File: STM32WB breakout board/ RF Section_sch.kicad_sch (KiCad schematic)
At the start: 12 parts, among them J3 RSP-122811-02

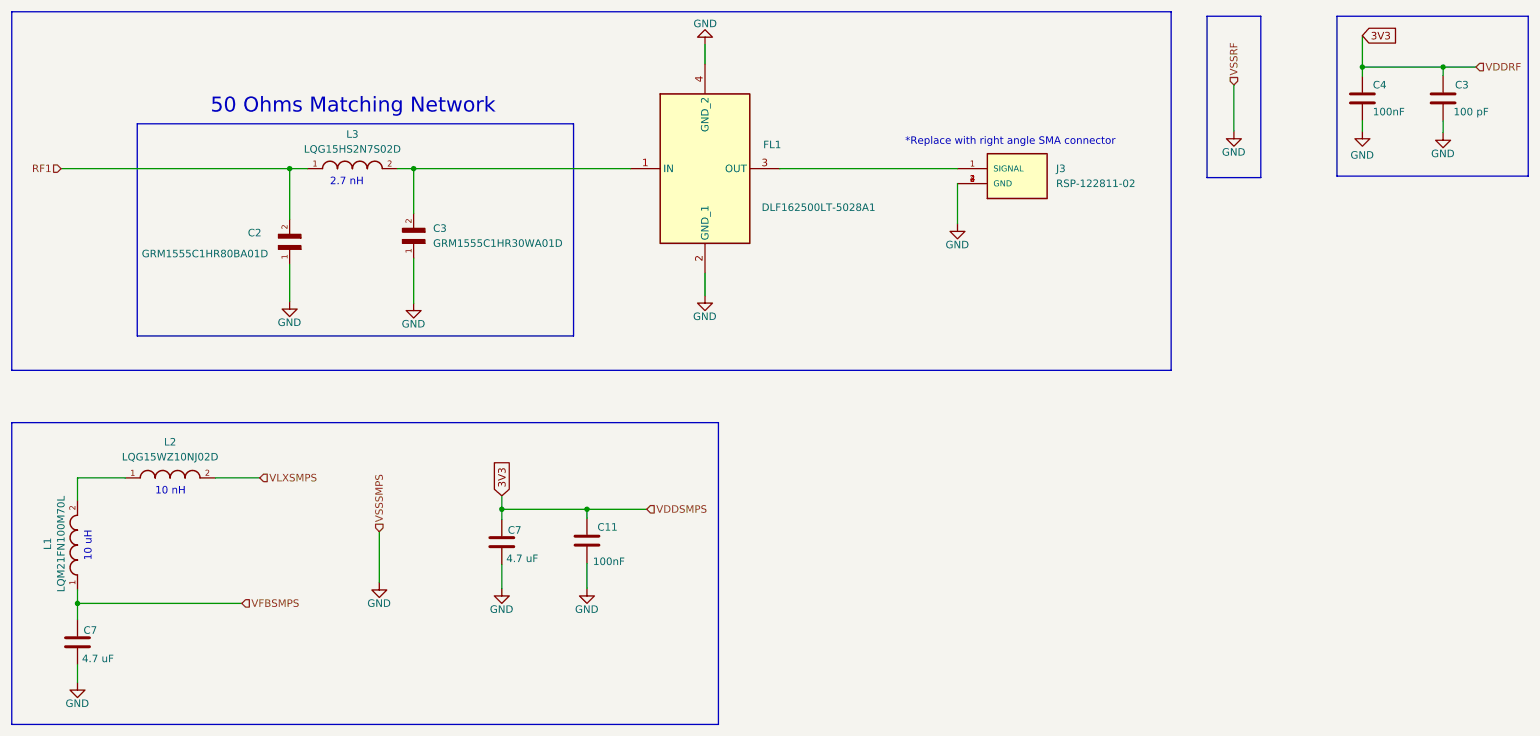
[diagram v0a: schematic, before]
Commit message: Regulator section updating
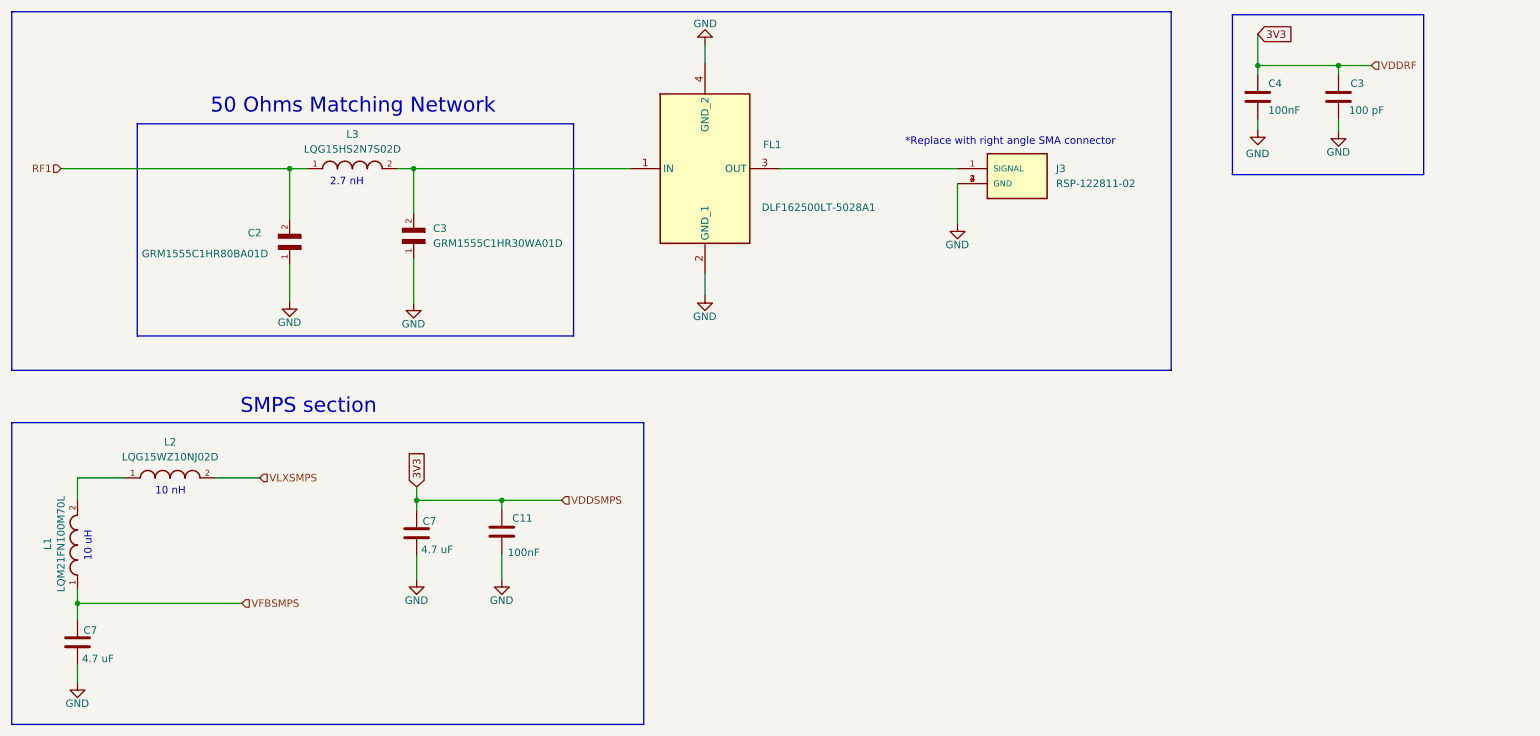
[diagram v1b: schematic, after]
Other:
- note added: "SMPS section"
- moved on the sheet: C11, C3, C4, C7

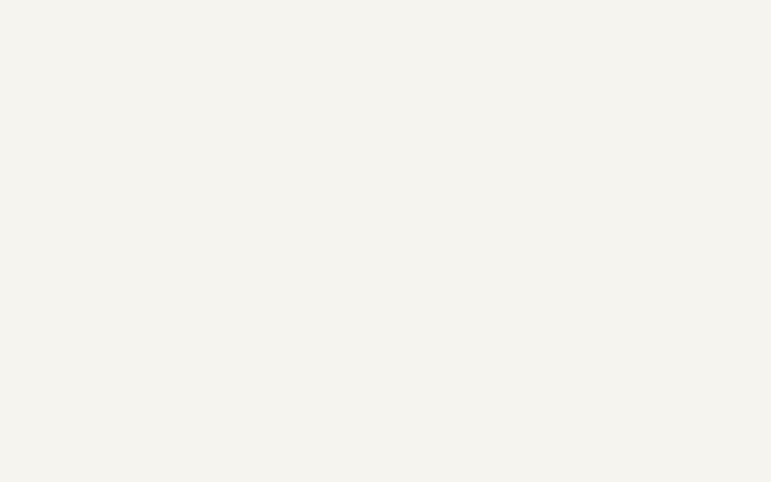
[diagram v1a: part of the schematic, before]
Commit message: Regulator section updating
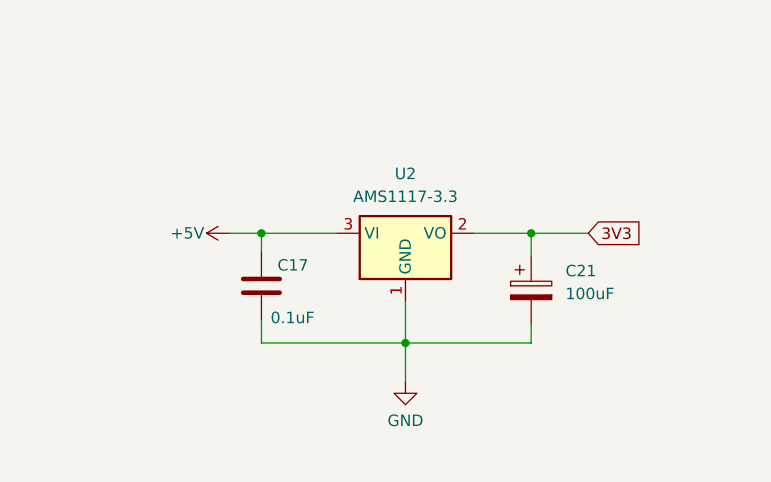
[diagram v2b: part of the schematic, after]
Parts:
- added C17: 0.1uF, Capacitor_SMD:C_0402_1005Metric, symbol Device:C
- added C21: 100uF, symbol Device:C_Polarized
- added U2: AMS1117-3.3, Package_TO_SOT_SMD:SOT-223-3_TabPin2, symbol Regulator_Linear:AMS1117-3.3
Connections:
- net 3V3: now also C21.1, U2.2 (VO)
- net GND: now also C17.2, C21.2, U2.1 (GND)
- new net +5V: C17.1, U2.3 (VI)
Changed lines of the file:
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@@
   (junction (at 68.072 46.99) (diameter 0) (color 0 0 0 0)
   )
+  (junction (at 236.22 115.824) (diameter 0) (color 0 0 0 0)
+  )
   (junction (at 89.154 46.99) (diameter 0) (color 0 0 0 0)
   )
   (junction (at 232.664 29.464) (diameter 0) (color 0 0 0 0)
   )
+  (junction (at 222.25 128.016) (diameter 0) (color 0 0 0 0)
+  )
+  (junction (at 206.248 115.824) (diameter 0) (color 0 0 0 0)
+  )
   (junction (at 89.662 103.378) (diameter 0) (color 0 0 0 0)
   )
@@
     (stroke (width 0) (type default))
   )
+  (wire (pts (xy 214.63 115.824) (xy 206.248 115.824))
+    (stroke (width 0) (type default))
+  )
   (wire (pts (xy 89.154 46.99) (xy 125.984 46.99))
     (stroke (width 0) (type default))
@@
     (stroke (width 0) (type default))
   )
+  (wire (pts (xy 202.692 115.824) (xy 206.248 115.824))
+    (stroke (width 0) (type default))
+  )
   (wire (pts (xy 232.664 38.608) (xy 232.664 40.386))
     (stroke (width 0) (type default))
@@
     (stroke (width 0) (type default))
   )
+  (wire (pts (xy 236.22 115.824) (xy 229.87 115.824))
+    (stroke (width 0) (type default))
+  )
   (wire (pts (xy 138.684 25.908) (xy 138.684 29.21))
     (stroke (width 0) (type default))
@@
     (stroke (width 0) (type default))
   )
+  (wire (pts (xy 206.248 128.016) (xy 222.25 128.016))
+    (stroke (width 0) (type default))
+  )
   (wire (pts (xy 89.154 62.23) (xy 89.154 69.85))
     (stroke (width 0) (type default))
@@
     (stroke (width 0) (type default))
   )
+  (wire (pts (xy 222.25 123.444) (xy 222.25 128.016))
+    (stroke (width 0) (type default))
+  )
   (wire (pts (xy 89.662 103.378) (xy 89.662 105.156))
     (stroke (width 0) (type default))
@@
     (stroke (width 0) (type default))
   )
+  (wire (pts (xy 236.22 125.984) (xy 236.22 128.016))
+    (stroke (width 0) (type default))
+  )
   (wire (pts (xy 246.38 29.464) (xy 251.968 29.464))
     (stroke (width 0) (type default))
@@
     (stroke (width 0) (type default))
   )
+  (wire (pts (xy 206.248 125.476) (xy 206.248 128.016))
+    (stroke (width 0) (type default))
+  )
   (wire (pts (xy 89.662 101.092) (xy 89.662 103.378))
     (stroke (width 0) (type default))
   )
+  (wire (pts (xy 236.22 128.016) (xy 222.25 128.016))
+    (stroke (width 0) (type default))
+  )
+  (wire (pts (xy 236.22 118.364) (xy 236.22 115.824))
+    (stroke (width 0) (type default))
+  )
+  (wire (pts (xy 236.22 115.824) (xy 242.57 115.824))
+    (stroke (width 0) (type default))
+  )
   (wire (pts (xy 104.14 104.902) (xy 104.14 103.378))
     (stroke (width 0) (type default))
   )
+  (wire (pts (xy 206.248 115.824) (xy 206.248 117.856))
+    (stroke (width 0) (type default))
+  )
   (wire (pts (xy 32.004 99.568) (xy 32.004 103.378))
+    (stroke (width 0) (type default))
+  )
+  (wire (pts (xy 222.25 128.016) (xy 222.25 132.334))
     (stroke (width 0) (type default))
   )
@@
   (text "10 uH" (at 34.544 113.792 90)
     (effects (font (size 1.27 1.27)) (justify left bottom))
+  )
+  (global_label "3V3" (shape input) (at 242.57 115.824 0) (fields_autoplaced)
+    (effects (font (size 1.27 1.27)) (justify left))
+    (property "Intersheetrefs" "${INTERSHEET_REFS}" (at 249.0628 115.824 0)
+      (effects (font (size 1.27 1.27)) (justify left) hide)
+    )
   )
   (global_label "3V3" (shape input) (at 232.664 24.13 0) (fields_autoplaced)
@@
     )
   )
+  (symbol (lib_id "power:GND") (at 222.25 132.334 0) (unit 1)
+    (in_bom yes) (on_board yes) (dnp no) (fields_autoplaced)
+    (property "Reference" "#PWR027" (at 222.25 138.684 0)
+      (effects (font (size 1.27 1.27)) hide)
+    )
+    (property "Value" "GND" (at 222.25 136.652 0)
+      (effects (font (size 1.27 1.27)))
+    )
+    (property "Footprint" "" (at 222.25 132.334 0)
+      (effects (font (size 1.27 1.27)) hide)
+    )
+    (property "Datasheet" "" (at 222.25 132.334 0)
+      (effects (font (size 1.27 1.27)) hide)
+    )
+    (pin "1")
+    (instances
+      (project "STM32WB breakout board"
+        (path "/29424def-bd0e-47af-8787-429d3d525da1/1e4823cc-51de-4557-be75-82cccb133913"
+          (reference "#PWR027") (unit 1)
+        )
+      )
+    )
+  )
   (symbol (lib_id "Device:C") (at 89.662 108.966 0) (unit 1)
     (in_bom yes) (on_board yes) (dnp no)
@@
         (path "/4ca0fb43-2fc5-4ba7-bade-b46629914b25"
           (reference "#PWR01") (unit 1)
+        )
+      )
+    )
+  )
+  (symbol (lib_id "Regulator_Linear:AMS1117-3.3") (at 222.25 115.824 0) (unit 1)
+    (in_bom yes) (on_board yes) (dnp no) (fields_autoplaced)
+    (property "Reference" "U2" (at 222.25 109.22 0)
+      (effects (font (size 1.27 1.27)))
+    )
+    (property "Value" "AMS1117-3.3" (at 222.25 111.76 0)
+      (effects (font (size 1.27 1.27)))
+    )
+    (property "Footprint" "Package_TO_SOT_SMD:SOT-223-3_TabPin2" (at 222.25 110.744 0)
+      (effects (font (size 1.27 1.27)) hide)
+    )
+    (property "Datasheet" "http://www.advanced-monolithic.com/pdf/ds1117.pdf" (at 224.79 122.174 0)
+      (effects (font (size 1.27 1.27)) hide)
+    )
+    (pin "1")
+    (pin "2")
+    (pin "3")
+    (instances
+      (project "STM32WB breakout board"
+        (path "/29424def-bd0e-47af-8787-429d3d525da1/1e4823cc-51de-4557-be75-82cccb133913"
+          (reference "U2") (unit 1)
         )
       )
@@
     )
   )
+  (symbol (lib_id "Device:C") (at 206.248 121.666 0) (unit 1)
+    (in_bom yes) (on_board yes) (dnp no)
+    (property "Reference" "C17" (at 208.026 119.38 0)
+      (effects (font (size 1.27 1.27)) (justify left))
+    )
+    (property "Value" "0.1uF" (at 207.264 125.222 0)
+      (effects (font (size 1.27 1.27)) (justify left))
+    )
+    (property "Footprint" "Capacitor_SMD:C_0402_1005Metric" (at 207.2132 125.476 0)
+      (effects (font (size 1.27 1.27)) hide)
+    )
+    (property "Datasheet" "~" (at 206.248 121.666 0)
+      (effects (font (size 1.27 1.27)) hide)
+    )
+    (pin "2")
+    (pin "1")
+    (instances
+      (project "STM32WB breakout board"
+        (path "/29424def-bd0e-47af-8787-429d3d525da1"
+          (reference "C17") (unit 1)
+        )
+        (path "/29424def-bd0e-47af-8787-429d3d525da1/1e4823cc-51de-4557-be75-82cccb133913"
+          (reference "C19") (unit 1)
+        )
+      )
+    )
+  )
   (symbol (lib_id "LQG15WZ10NJ02D:LQG15WZ10NJ02D") (at 47.752 99.568 0) (unit 1)
     (in_bom yes) (on_board yes) (dnp no) (fields_autoplaced)
@@
     )
   )
+  (symbol (lib_id "Device:C_Polarized") (at 236.22 122.174 0) (unit 1)
+    (in_bom yes) (on_board yes) (dnp no) (fields_autoplaced)
+    (property "Reference" "C21" (at 240.03 120.015 0)
+      (effects (font (size 1.27 1.27)) (justify left))
+    )
+    (property "Value" "100uF" (at 240.03 122.555 0)
+      (effects (font (size 1.27 1.27)) (justify left))
+    )
+    (property "Footprint" "" (at 237.1852 125.984 0)
+      (effects (font (size 1.27 1.27)) hide)
+    )
+    (property "Datasheet" "~" (at 236.22 122.174 0)
+      (effects (font (size 1.27 1.27)) hide)
+    )
+    (pin "2")
+    (pin "1")
+    (instances
+      (project "STM32WB breakout board"
+        (path "/29424def-bd0e-47af-8787-429d3d525da1/1e4823cc-51de-4557-be75-82cccb133913"
+          (reference "C21") (unit 1)
+        )
+      )
+    )
+  )
   (symbol (lib_id "power:GND") (at 232.664 40.386 0) (unit 1)
     (in_bom yes) (on_board yes) (dnp no)
@@
         )
       )
+    )
+  )
+  (symbol (lib_id "power:+5V") (at 202.692 115.824 90) (unit 1)
+    (in_bom yes) (on_board yes) (dnp no)
+    (property "Reference" "#PWR028" (at 206.502 115.824 0)
+      (effects (font (size 1.27 1.27)) hide)
+    )
+    (property "Value" "+5V" (at 199.898 115.824 90)
+      (effects (font (size 1.27 1.27)) (justify left))
+    )
+    (property "Footprint" "" (at 202.692 115.824 0)
+      (effects (font (size 1.27 1.27)) hide)
+    )
+    (property "Datasheet" "" (at 202.692 115.824 0)
+      (effects (font (size 1.27 1.27)) hide)
+    )
+    (pin "1")
+    (instances
+      (project "STM32WB breakout board"
+        (path "/29424def-bd0e-47af-8787-429d3d525da1/1e4823cc-51de-4557-be75-82cccb133913"
+          (reference "#PWR028") (unit 1)
+        )
+      )

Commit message: Regulator section updating
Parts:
- C21: footprint (none) -> Capacitor_SMD:C_0402_1005Metric
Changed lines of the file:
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@@
       (effects (font (size 1.27 1.27)) (justify left))
     )
-    (property "Footprint" "" (at 237.1852 125.984 0)
+    (property "Footprint" "Capacitor_SMD:C_0402_1005Metric" (at 237.1852 125.984 0)
       (effects (font (size 1.27 1.27)) hide)
     )

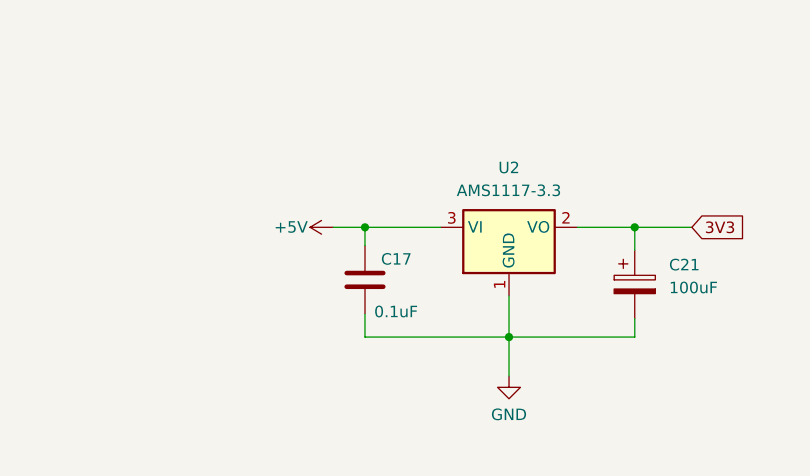
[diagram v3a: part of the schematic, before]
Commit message: Regulator section updating
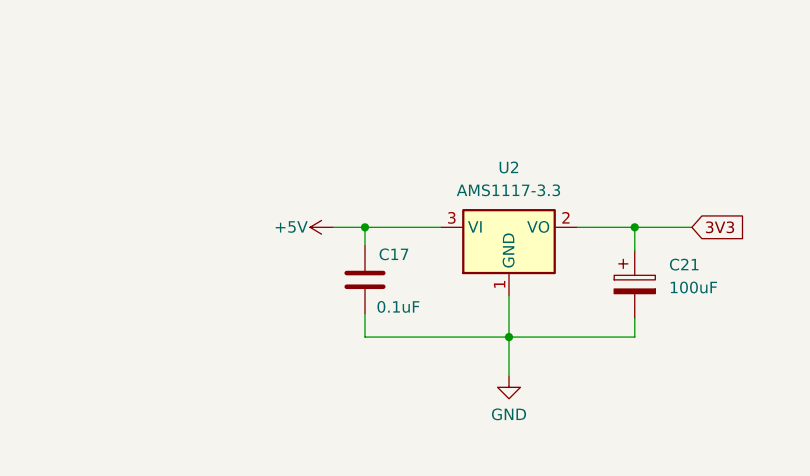
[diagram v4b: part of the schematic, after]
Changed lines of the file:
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@@
   (symbol (lib_id "Device:C") (at 206.248 121.666 0) (unit 1)
     (in_bom yes) (on_board yes) (dnp no)
-    (property "Reference" "C17" (at 208.026 119.38 0)
+    (property "Reference" "C17" (at 207.772 118.872 0)
       (effects (font (size 1.27 1.27)) (justify left))
     )
-    (property "Value" "0.1uF" (at 207.264 125.222 0)
+    (property "Value" "0.1uF" (at 207.518 124.714 0)
       (effects (font (size 1.27 1.27)) (justify left))
     )

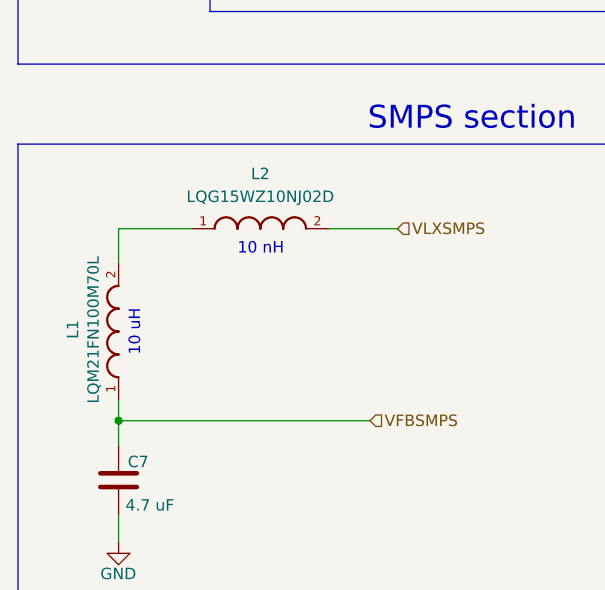
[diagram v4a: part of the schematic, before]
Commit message: SMD resistors updated, some issue with inductor footprint
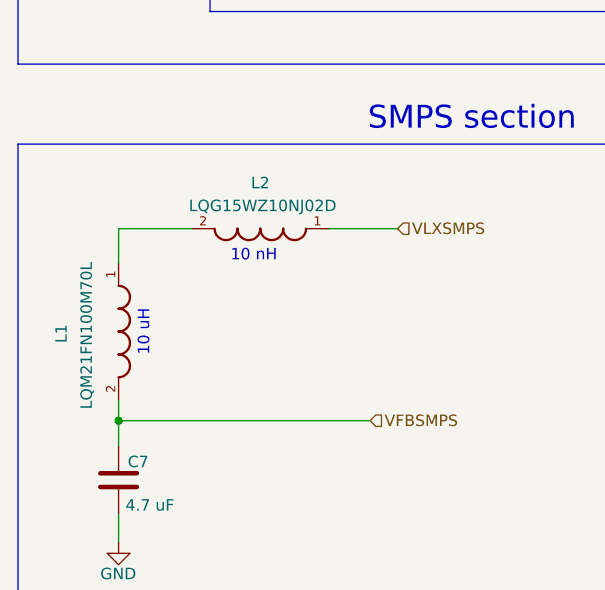
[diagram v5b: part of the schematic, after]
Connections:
- net VFBSMPS: now also L1.2; no longer L1.1
- net VLXSMPS: now also L2.1; no longer L2.2
- new net: L1.1, L2.2
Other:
- moved on the sheet: L1, L2
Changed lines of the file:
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@@
     (effects (font (size 1.27 1.27)) (justify left bottom))
   )
-  (text "10 nH\n" (at 45.212 102.616 0)
+  (text "10 nH\n" (at 44.45 103.378 0)
     (effects (font (size 1.27 1.27)) (justify left bottom))
   )
@@
     (effects (font (size 2.54 2.54)) (justify left bottom))
   )
-  (text "10 uH" (at 34.544 113.792 90)
+  (text "10 uH" (at 35.56 113.792 90)
     (effects (font (size 1.27 1.27)) (justify left bottom))
   )
@@
     )
   )
-  (symbol (lib_id "LQM21FN100M70L:LQM21FN100M70L") (at 32.004 110.998 90) (unit 1)
-    (in_bom yes) (on_board yes) (dnp no)
-    (property "Reference" "L1" (at 26.924 109.728 0)
+  (symbol (lib_id "LQM21FN100M70L:LQM21FN100M70L") (at 32.004 110.998 270) (unit 1)
+    (in_bom yes) (on_board yes) (dnp no)
+    (property "Reference" "L1" (at 25.654 112.268 0)
       (effects (font (size 1.27 1.27)) (justify right))
     )
-    (property "Value" "LQM21FN100M70L" (at 29.21 102.616 0)
+    (property "Value" "LQM21FN100M70L" (at 28.448 119.634 0)
       (effects (font (size 1.27 1.27)) (justify right))
     )
@@
     )
   )
-  (symbol (lib_id "LQG15WZ10NJ02D:LQG15WZ10NJ02D") (at 47.752 99.568 0) (unit 1)
-    (in_bom yes) (on_board yes) (dnp no) (fields_autoplaced)
-    (property "Reference" "L2" (at 47.752 93.472 0)
+  (symbol (lib_id "LQG15WZ10NJ02D:LQG15WZ10NJ02D") (at 47.752 99.568 180) (unit 1)
+    (in_bom yes) (on_board yes) (dnp no)
+    (property "Reference" "L2" (at 47.752 94.488 0)
       (effects (font (size 1.27 1.27)))
     )
-    (property "Value" "LQG15WZ10NJ02D" (at 47.752 96.012 0)
+    (property "Value" "LQG15WZ10NJ02D" (at 48.006 97.028 0)
       (effects (font (size 1.27 1.27)))
     )

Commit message: L3 footprint updated
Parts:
- L3: footprint LQG15HS2N7S02D:INDC1005X55N -> Inductor_SMD:L_0402_1005Metric
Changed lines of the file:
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@@
       (effects (font (size 1.27 1.27)))
     )
-    (property "Footprint" "LQG15HS2N7S02D:INDC1005X55N" (at 78.74 46.99 0)
+    (property "Footprint" "Inductor_SMD:L_0402_1005Metric" (at 78.74 46.99 0)
       (effects (font (size 1.27 1.27)) (justify bottom) hide)
     )

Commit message: AMS1117 updated
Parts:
- C17: footprint Capacitor_SMD:C_0402_1005Metric -> Capacitor_THT:C_Disc_D6.0mm_W2.5mm_P5.00mm
- C21: footprint Capacitor_SMD:C_0402_1005Metric -> Capacitor_THT:CP_Radial_D8.0mm_P3.50mm
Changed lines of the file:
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@@
       (effects (font (size 1.27 1.27)) (justify left))
     )
-    (property "Footprint" "Capacitor_SMD:C_0402_1005Metric" (at 207.2132 125.476 0)
+    (property "Footprint" "Capacitor_THT:C_Disc_D6.0mm_W2.5mm_P5.00mm" (at 207.2132 125.476 0)
       (effects (font (size 1.27 1.27)) hide)
     )
@@
       (effects (font (size 1.27 1.27)) (justify left))
     )
-    (property "Footprint" "Capacitor_SMD:C_0402_1005Metric" (at 237.1852 125.984 0)
-      (effects (font (size 1.27 1.27)) hide)
-    )
+    (property "Footprint" "Capacitor_THT:CP_Radial_D8.0mm_P3.50mm" (at 237.1852 125.984 0)
+      (effects (font (size 1.27 1.27)) hide)
+    )
